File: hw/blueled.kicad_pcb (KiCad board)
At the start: 2 copper layers, 54 x 85.6 mm, 62 parts, among them J1 Barrel_Jack, J2 LED Strip, J3 ICSP, J4 Screw_Terminal_01x02, Q1 Q_PMOS_SDG, Q2 Q_PNP_EBC, Q3 BSS138, SW2 PUSH, U1 ATmega328P-AU, U2 HC-05, U3 AMS1117-3.3, U4 AT25SF081, U5 LM25085MM, X1 CSTCE

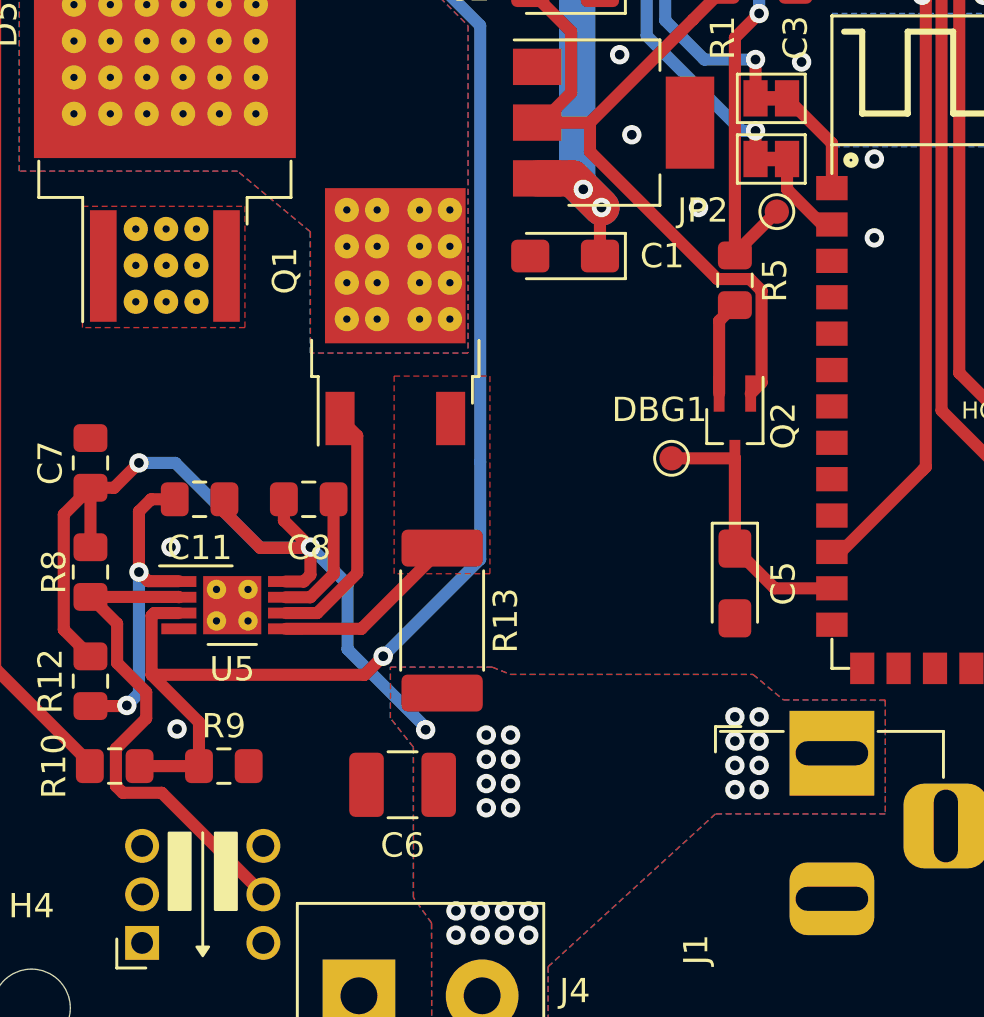
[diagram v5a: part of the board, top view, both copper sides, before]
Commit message: fix(hw): change input cap + minor fixes
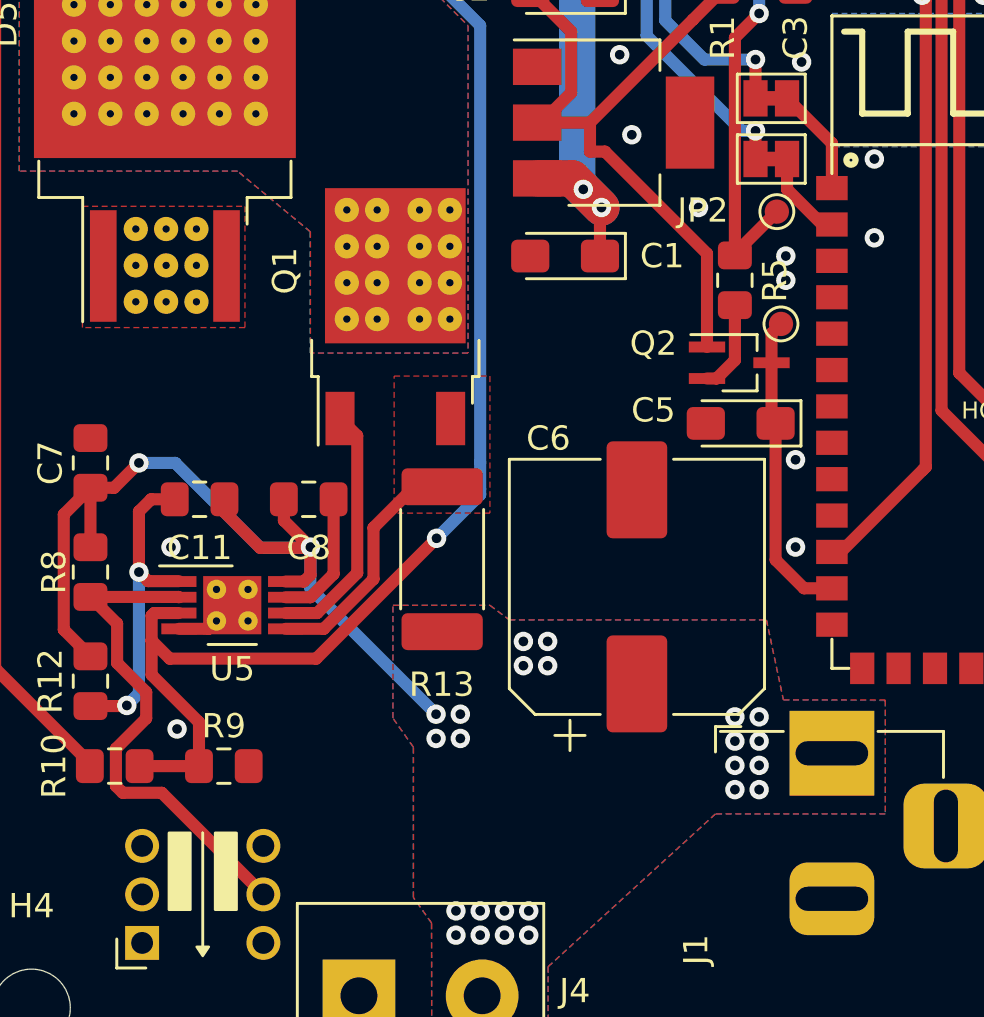
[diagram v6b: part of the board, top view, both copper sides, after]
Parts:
- C6: value 4.7uF -> 33uF; footprint Capacitor_SMD:C_1210_3225Metric_Pad1.42x2.65mm_HandSolder -> Capacitor_SMD:CP_Elec_10x10
- moved C6 12.6 mm to (148.5, 127.6), turned to 90 degrees
- moved DBG1 7.14 mm to (154.4, 116.8)
- moved C5 6.60 mm to (152.7, 120.9), turned to 180 degrees
- moved Q2 2.61 mm to (152.7, 118.4), turned to 0 degrees
- moved R13 2.53 mm to (140.4, 126.5)
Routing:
- net +3V3: track 118.0 -> 114.6 mm
- net GND: track 13.8 -> 16.4 mm, vias 24 -> 28
- net Net-(Q1-Pad1): track 7.83 -> 10.1 mm
- net Net-(C5-Pad1): track 11.0 -> 12.8 mm
- net Net-(C9-Pad2): track 63.3 -> 61.7 mm
- net /VINJACK: track 40.2 -> 39.7 mm, vias 27 -> 26
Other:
- board text added: "C6 (input bulk cap) + D5 + MOSFET loop has to be small"
- board text added: "This vias voodoo is questinable but could help with heat dissipation"

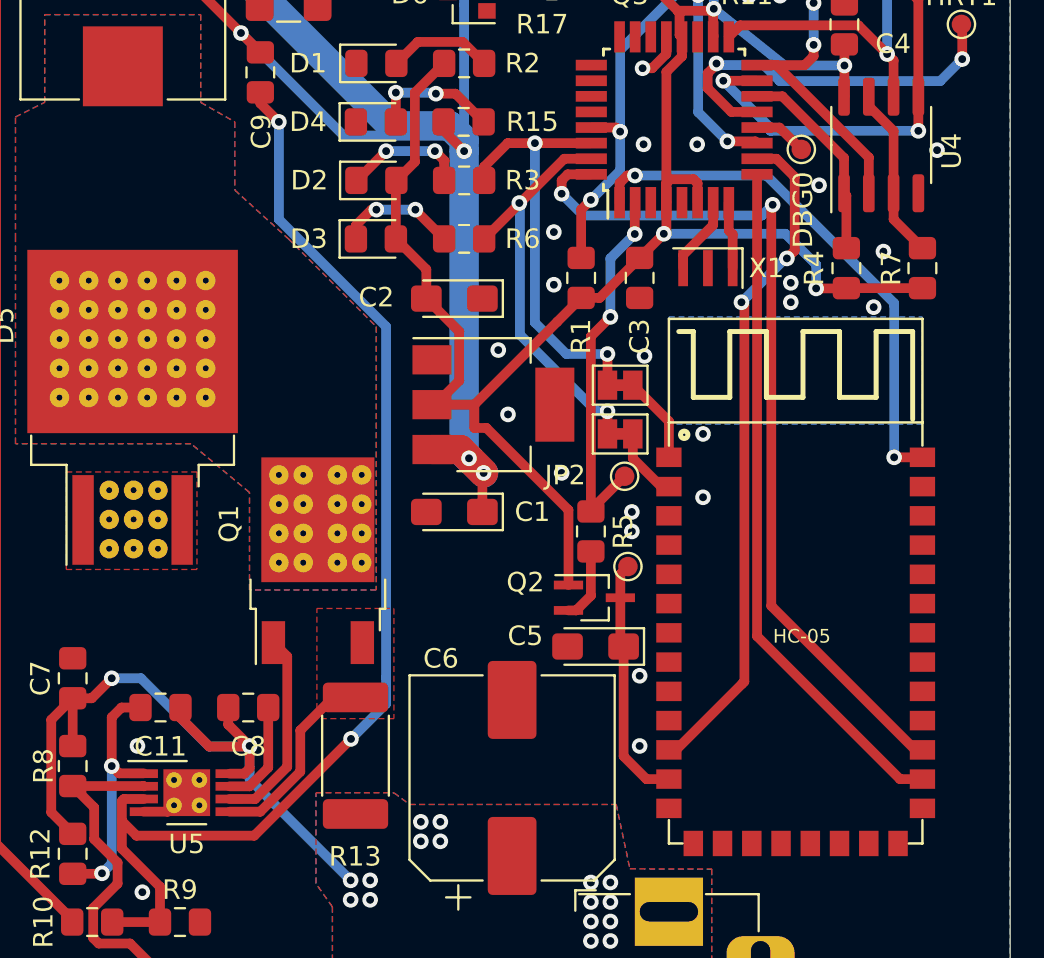
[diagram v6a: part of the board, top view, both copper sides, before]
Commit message: fix(hw): minor adjustments (shorter current loop)
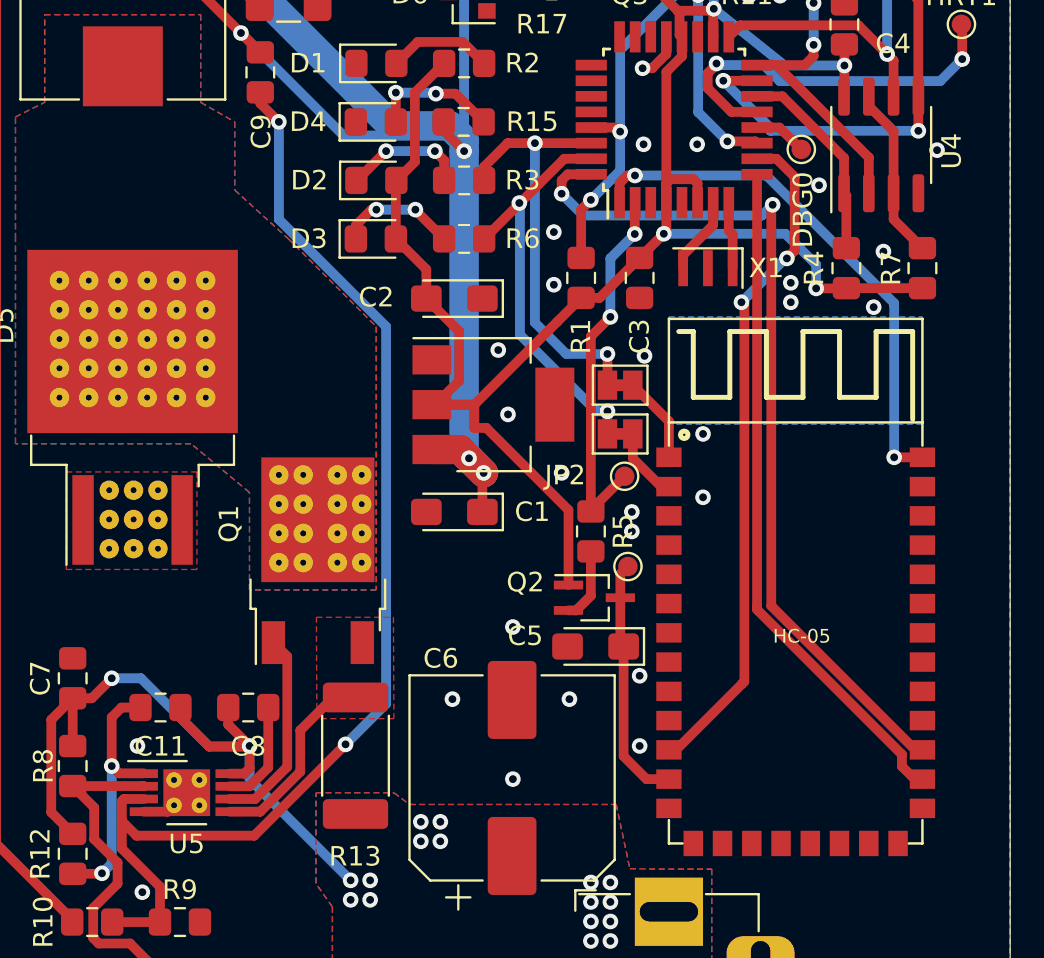
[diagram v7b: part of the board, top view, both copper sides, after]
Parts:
- D2: value LED -> RX
- D3: value LED -> TX
- J1: value Barrel_Jack -> DC 5.5 - 42V
- J4: value Screw_Terminal_01x02 -> DC 5.5 - 42V
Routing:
- net GND: vias 28 -> 32
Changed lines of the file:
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@@
     (thickness 1.6)
     (drawings 15)
-    (tracks 481)
+    (tracks 486)
     (zones 0)
     (modules 62)
@@
     (46 B.CrtYd user)
     (47 F.CrtYd user)
-    (48 B.Fab user hide)
-    (49 F.Fab user hide)
+    (48 B.Fab user)
+    (49 F.Fab user)
   )
   (setup
@@
       (effects (font (size 1 1) (thickness 0.15)))
     )
-    (fp_text value Screw_Terminal_01x02 (at 2.54 5.08) (layer F.Fab)
+    (fp_text value "DC 5.5 - 42V" (at 2.54 5.08) (layer F.Fab)
       (effects (font (size 1 1) (thickness 0.15)))
     )
@@
       (effects (font (size 1 1) (thickness 0.15)))
     )
-    (fp_text value Barrel_Jack (at -6.2 -5.5 90) (layer F.Fab)
+    (fp_text value "DC 5.5 - 42V" (at -6.2 -5.5 90) (layer F.Fab)
       (effects (font (size 1 1) (thickness 0.15)))
     )
@@
       (effects (font (size 1 1) (thickness 0.15)))
     )
-    (fp_text value LED (at 0 1.65) (layer F.Fab)
+    (fp_text value TX (at 0 1.65) (layer F.Fab)
       (effects (font (size 1 1) (thickness 0.15)))
     )
@@
       (effects (font (size 1 1) (thickness 0.15)))
     )
-    (fp_text value LED (at 0 1.65) (layer F.Fab)
+    (fp_text value RX (at 0 1.65) (layer F.Fab)
       (effects (font (size 1 1) (thickness 0.15)))
     )
@@
   (via (at 155 126) (size 0.8) (drill 0.4) (layers F.Cu B.Cu) (net 4))
   (via (at 154.6 115) (size 0.8) (drill 0.4) (layers F.Cu B.Cu) (net 4))
+  (via (at 148.5 127.7) (size 0.8) (drill 0.4) (layers F.Cu B.Cu) (net 4))
+  (via (at 145.4 123.6) (size 0.8) (drill 0.4) (layers F.Cu B.Cu) (net 4))
+  (via (at 151.4 123.6) (size 0.8) (drill 0.4) (layers F.Cu B.Cu) (net 4))
+  (via (at 148.5 119.9) (size 0.8) (drill 0.4) (layers F.Cu B.Cu) (net 4))
   (segment (start 140.475 97) (end 140.5 97) (width 0.5) (layer F.Cu) (net 5) (status 30))
   (via (at 142 95.5) (size 0.8) (drill 0.4) (layers F.Cu B.Cu) (net 5))
@@
   (segment (start 162.949999 100.600001) (end 162.949999 96.824997) (width 0.5) (layer F.Cu) (net 20))
   (segment (start 162.55 101) (end 162.949999 100.600001) (width 0.5) (layer F.Cu) (net 20))
-  (segment (start 161.02 120.37) (end 161.02 96.69) (width 0.5) (layer F.Cu) (net 21) (status 20))
-  (segment (start 168.35 127.7) (end 161.02 120.37) (width 0.5) (layer F.Cu) (net 21))
-  (segment (start 169.5 127.7) (end 168.35 127.7) (width 0.5) (layer F.Cu) (net 21) (status 10))
+  (segment (start 169.5 127.7) (end 169.1 127.7) (width 0.5) (layer F.Cu) (net 21))
+  (segment (start 169.1 127.7) (end 168.449999 127.049999) (width 0.5) (layer F.Cu) (net 21))
+  (segment (start 161.02 119.009254) (end 161.02 118.82) (width 0.5) (layer F.Cu) (net 21))
+  (segment (start 168.449999 126.439253) (end 161.02 119.009254) (width 0.5) (layer F.Cu) (net 21))
+  (segment (start 168.449999 127.049999) (end 168.449999 126.439253) (width 0.5) (layer F.Cu) (net 21))
+  (segment (start 161.02 118.82) (end 161.02 96.69) (width 0.5) (layer F.Cu) (net 21))
   (segment (start 169.5 111.2) (end 168.05 111.2) (width 0.5) (layer F.Cu) (net 22) (status 10))
   (via (at 168.05 111.2) (size 0.8) (drill 0.4) (layers F.Cu B.Cu) (net 22))
@@
   (segment (start 135.55 93.05) (end 136.5 94) (width 0.5) (layer F.Cu) (net 30) (status 10))
   (via (at 136.5 94) (size 0.8) (drill 0.4) (layers F.Cu B.Cu) (net 30))
-  (segment (start 136.5 94) (end 136.5 99) (width 0.5) (layer B.Cu) (net 30))
-  (segment (start 136.5 99) (end 142 104.5) (width 0.5) (layer B.Cu) (net 30))
-  (segment (start 142 104.5) (end 142 122.5) (width 0.5) (layer B.Cu) (net 30))
   (segment (start 130.405 133.220998) (end 130.405 135.03) (width 0.5) (layer F.Cu) (net 30))
   (segment (start 128.451 131.266998) (end 130.405 133.220998) (width 0.5) (layer F.Cu) (net 30))
@@
   (segment (start 129.576001 128.720001) (end 128.555999 128.720001) (width 0.5) (layer F.Cu) (net 30))
   (segment (start 128.451 128.825) (end 128.451 129.851) (width 0.5) (layer F.Cu) (net 30))
-  (segment (start 128.451 129.851) (end 129.2 130.6) (width 0.5) (layer F.Cu) (net 30))
   (segment (start 128.451 129.851) (end 128.451 131.266998) (width 0.5) (layer F.Cu) (net 30))
-  (segment (start 129.2 130.6) (end 135.238504 130.6) (width 0.5) (layer F.Cu) (net 30))
-  (segment (start 135.238504 130.6) (end 140.2 125.638504) (width 0.5) (layer F.Cu) (net 30))
-  (via (at 140.2 125.638504) (size 0.8) (drill 0.4) (layers F.Cu B.Cu) (net 30))
-  (segment (start 142 123.838504) (end 142 123.6) (width 0.5) (layer B.Cu) (net 30))
-  (segment (start 140.2 125.638504) (end 142 123.838504) (width 0.5) (layer B.Cu) (net 30))
-  (segment (start 142 122.5) (end 142 123.6) (width 0.5) (layer B.Cu) (net 30))
+  (segment (start 136.5 99) (end 136.5 94) (width 0.5) (layer B.Cu) (net 30))
+  (segment (start 142 104.5) (end 136.5 99) (width 0.5) (layer B.Cu) (net 30))
+  (segment (start 142 123.838504) (end 142 104.5) (width 0.5) (layer B.Cu) (net 30))
+  (segment (start 139.919252 125.919252) (end 142 123.838504) (width 0.5) (layer B.Cu) (net 30))
+  (segment (start 129.2 130.6) (end 128.451 129.851) (width 0.5) (layer F.Cu) (net 30))
+  (segment (start 135.238504 130.6) (end 129.2 130.6) (width 0.5) (layer F.Cu) (net 30))
+  (segment (start 139.919252 125.919252) (end 135.238504 130.6) (width 0.5) (layer F.Cu) (net 30))
+  (via (at 139.919252 125.919252) (size 0.8) (drill 0.4) (layers F.Cu B.Cu) (net 30))
   (segment (start 135.5125 87.5) (end 135.5125 82.5) (width 0.5) (layer F.Cu) (net 31) (status 30))
   (segment (start 135.5125 80.0125) (end 137.525 78) (width 0.5) (layer F.Cu) (net 31) (status 20))
@@
     (polygon
       (pts
-        (xy 142.4 124.6) (xy 138.45 124.6) (xy 138.45 118.95) (xy 142.4 118.95)
+        (xy 142.4 124.6) (xy 138.45 124.6) (xy 138.425 119.4) (xy 142.375 119.4)
       )
     )

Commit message: add(hw): labels and 3D models
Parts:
- added G***: LOGO, blueled:hexagon-logo, F.Cu at (146.5, 84.2)
- added REF**: OSHW-Logo2_14.6x12mm_SilkScreen, Symbol:OSHW-Logo2_14.6x12mm_SilkScreen, B.Cu at (132.1, 71.0)
- DC 5.5 - 42V: renamed from J1
- renumbered D1 to 3.3, D4 to 5V, HRT1 to HRT, J3 to ISP, SW2 to RST, D2 to RX, D3 to TX, JP2 to TX
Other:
- board text added: "https://github.com/alberand/blueled"
